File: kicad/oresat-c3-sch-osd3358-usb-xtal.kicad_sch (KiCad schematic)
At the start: 36 parts, among them U1 OSD3358-512M-BSM, U11 RCLAMP0504FB, Y1 24MHz, Y2 Crystal

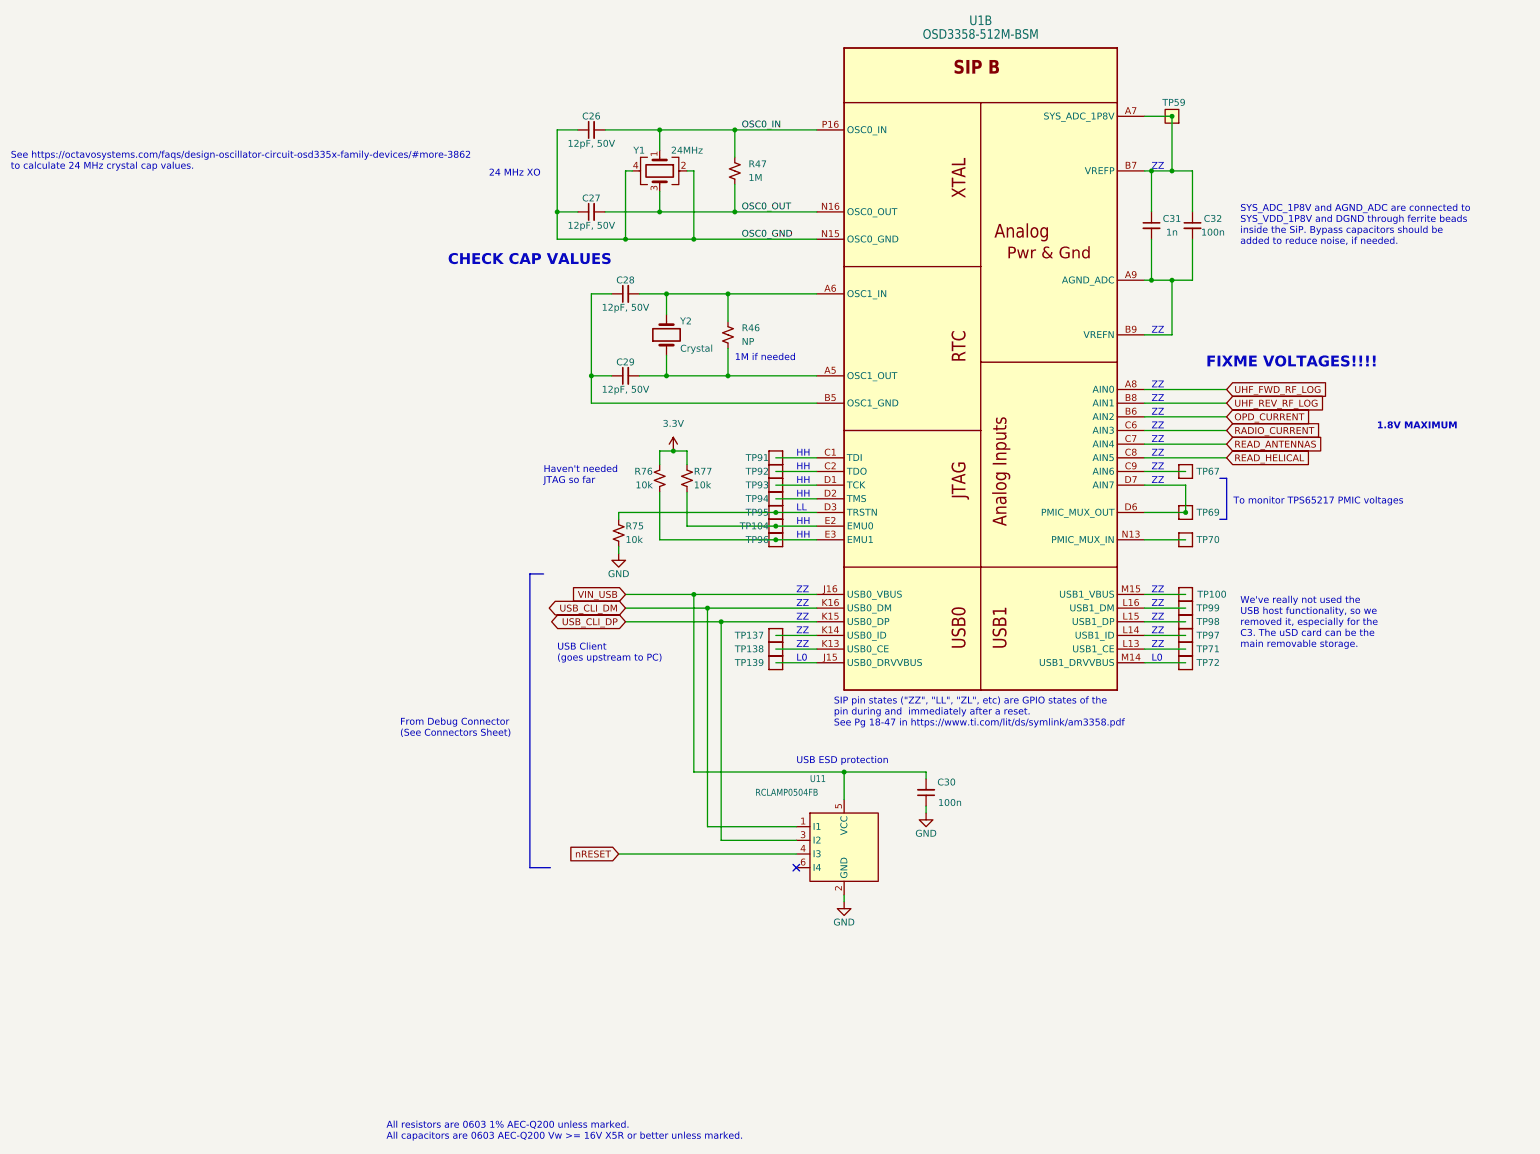
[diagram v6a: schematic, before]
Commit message: More fixes. TOT_CLEAR moved to a non HH pin, cleaned up in2 zones, moved fiducials, set dv/dt on power switches, added HW ID (5 bits) rechecked ADC 1.8V limits and fixed resistor values to match.
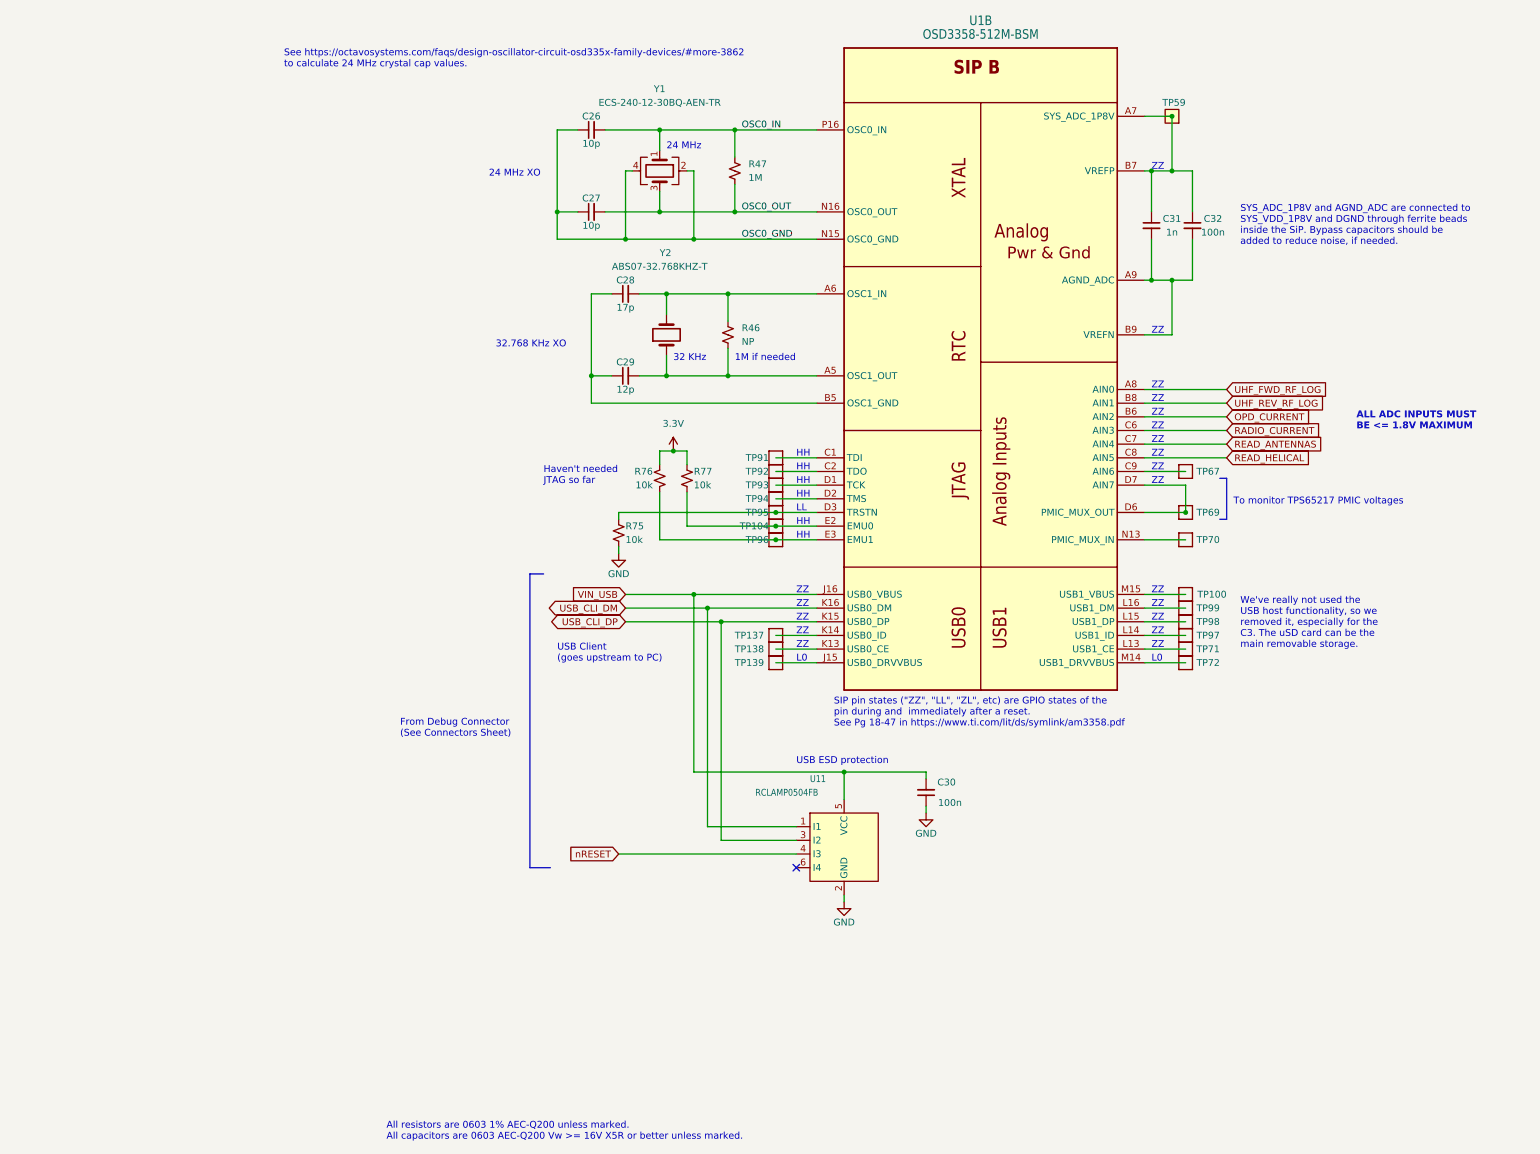
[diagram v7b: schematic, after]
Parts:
- C26, C27: value 12pF, 50V -> 10p
- C28: value 12pF, 50V -> 17p
- C29: value 12pF, 50V -> 12p
- Y1: value 24MHz -> ECS-240-12-30BQ-AEN-TR
- Y2: value Crystal -> ABS07-32.768KHZ-T
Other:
- note added: "24 MHz"
- note added: "32 KHz"
- note added: "32.768 KHz XO"
- note added: "ALL ADC INPUTS MUST BE <= 1.8V MAXIMUM"
- note removed: "1.8V MAXIMUM"
- note removed: "CHECK CAP VALUES"
- note removed: "FIXME VOLTAGES!!!!"
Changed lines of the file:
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@@
     (effects (font (size 1.27 1.27)) (justify left bottom))
   )
-  (text "1.8V MAXIMUM" (at 299.72 129.54 0)
+  (text "32.768 KHz XO" (at 135.89 114.3 0)
+    (effects (font (size 1.27 1.27)) (justify left bottom))
+  )
+  (text "ALL ADC INPUTS MUST\nBE <= 1.8V MAXIMUM" (at 295.91 129.54 0)
     (effects (font (size 1.27 1.27) (thickness 0.254) bold) (justify left bottom))
   )
@@
   (text "ZZ" (at 257.81 160.02 0)
     (effects (font (size 1.27 1.27)) (justify left bottom))
-  )
-  (text "FIXME VOLTAGES!!!!" (at 267.97 118.11 0)
-    (effects (font (size 2 2) (thickness 0.4) bold (color 255 0 0 1)) (justify left bottom))
   )
   (text "ZZ" (at 257.81 132.08 0)
@@
   )
   (text "See https://octavosystems.com/faqs/design-oscillator-circuit-osd335x-family-devices/#more-3862\nto calculate 24 MHz crystal cap values."
-    (at 45.72 81.28 0)
+    (at 96.52 62.23 0)
     (effects (font (size 1.27 1.27)) (justify left bottom))
   )
@@
     (effects (font (size 1.27 1.27)) (justify left bottom))
   )
-  (text "CHECK CAP VALUES" (at 127 99.06 0)
-    (effects (font (size 2 2) (thickness 0.4) bold (color 255 0 0 1)) (justify left bottom))
-  )
   (text "1M if needed" (at 180.34 116.84 0)
     (effects (font (size 1.27 1.27)) (justify left bottom))
@@
     (effects (font (size 1.27 1.27)) (justify left bottom))
   )
+  (text "32 KHz" (at 168.91 116.84 0)
+    (effects (font (size 1.27 1.27)) (justify left bottom))
+  )
   (text "HH" (at 191.77 134.62 0)
     (effects (font (size 1.27 1.27) (color 255 0 0 1)) (justify left bottom))
@@
   )
   (text "ZZ" (at 191.77 167.64 0)
+    (effects (font (size 1.27 1.27)) (justify left bottom))
+  )
+  (text "24 MHz" (at 167.64 77.47 0)
     (effects (font (size 1.27 1.27)) (justify left bottom))
   )
@@
   (symbol (lib_id "Device:Crystal_GND24") (at 166.37 81.28 270) (unit 1)
     (in_bom yes) (on_board yes) (dnp no)
-    (property "Reference" "Y1" (at 162.56 77.47 90)
-      (effects (font (size 1.27 1.27)))
-    )
-    (property "Value" "24MHz" (at 171.45 77.47 90)
+    (property "Reference" "Y1" (at 166.37 66.04 90)
+      (effects (font (size 1.27 1.27)))
+    )
+    (property "Value" "ECS-240-12-30BQ-AEN-TR" (at 166.37 68.58 90)
       (effects (font (size 1.27 1.27)))
     )
@@
       (effects (font (size 1.27 1.27)) hide)
     )
-    (property "Datasheet" "~" (at 166.37 81.28 0)
+    (property "Datasheet" "https://ecsxtal.com/store/pdf/ECX-53BQ.pdf" (at 166.37 81.28 0)
       (effects (font (size 1.27 1.27)) hide)
     )
@@
   (symbol (lib_id "Device:Crystal") (at 167.64 111.76 90) (unit 1)
     (in_bom yes) (on_board yes) (dnp no)
-    (property "Reference" "Y2" (at 170.18 109.22 90)
+    (property "Reference" "Y2" (at 166.37 96.52 90)
       (effects (font (size 1.27 1.27)) (justify right))
     )
-    (property "Value" "Crystal" (at 170.18 114.3 90)
+    (property "Value" "ABS07-32.768KHZ-T" (at 157.48 99.06 90)
       (effects (font (size 1.27 1.27)) (justify right))
     )
@@
       (effects (font (size 1.27 1.27)) hide)
     )
-    (property "Datasheet" "~" (at 167.64 111.76 0)
+    (property "Datasheet" "https://abracon.com/Resonators/ABS07.pdf" (at 167.64 111.76 0)
       (effects (font (size 1.27 1.27)) hide)
     )
@@
       (effects (font (size 1.27 1.27)))
     )
-    (property "Value" "12pF, 50V" (at 153.67 91.44 90)
+    (property "Value" "10p" (at 153.67 91.44 90)
       (effects (font (size 1.27 1.27)))
     )
@@
       (effects (font (size 1.27 1.27)))
     )
-    (property "Value" "12pF, 50V" (at 160.02 121.92 90)
+    (property "Value" "12p" (at 160.02 121.92 90)
       (effects (font (size 1.27 1.27)))
     )
@@
       (effects (font (size 1.27 1.27)))
     )
-    (property "Value" "12pF, 50V" (at 160.02 106.68 90)
+    (property "Value" "17p" (at 160.02 106.68 90)
       (effects (font (size 1.27 1.27)))
     )
@@
       (effects (font (size 1.27 1.27)))
     )
-    (property "Value" "12pF, 50V" (at 153.67 76.2 90)
-      (effects (font (size 1.27 1.27)))
-    )
+    (property "Value" "10p" (at 153.67 76.2 90)
+      (effects (font (size 1.27 1.27)))
+    )

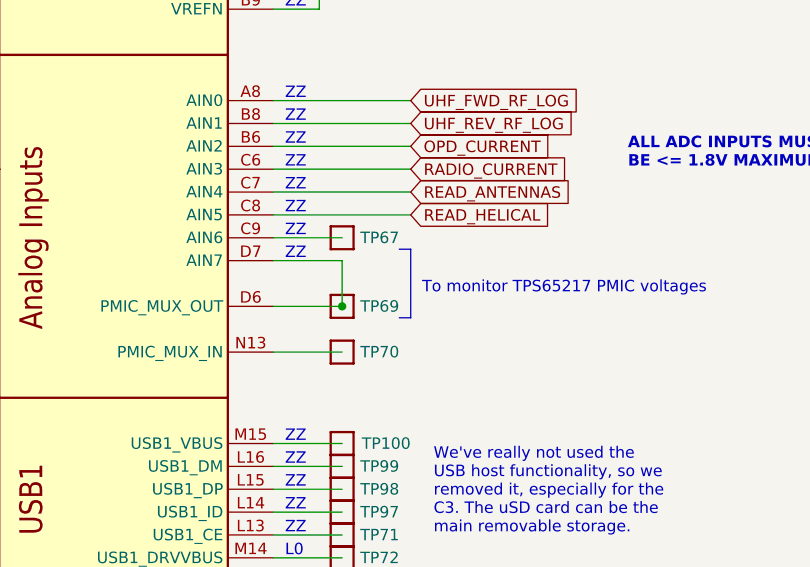
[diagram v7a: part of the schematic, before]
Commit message: Updated AX5043 foot print, moved synthesize to correct L length, fixed more grounds
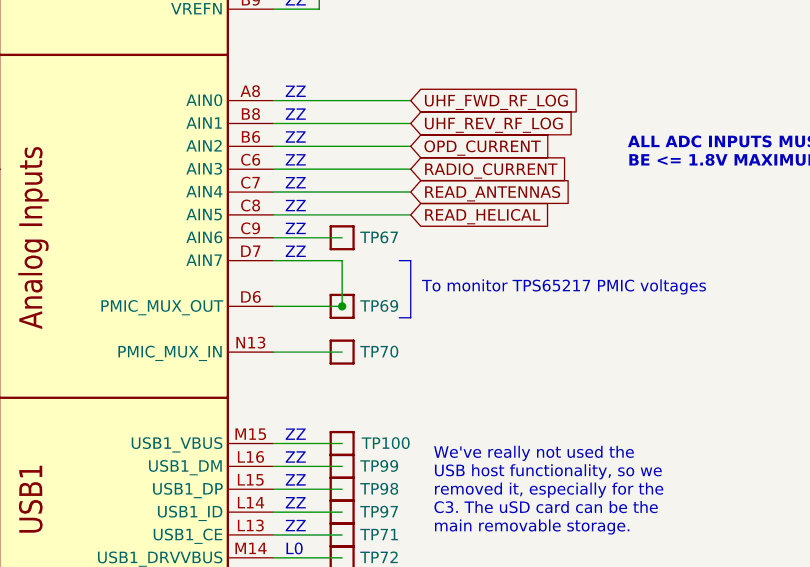
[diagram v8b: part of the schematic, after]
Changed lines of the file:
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@@
   )
   (no_connect (at 191.77 210.82))
-  (polyline (pts (xy 271.78 138.43) (xy 271.78 146.05))
+  (polyline (pts (xy 271.78 139.7) (xy 271.78 146.05))
     (stroke (width 0) (type default))
   )
@@
     (stroke (width 0) (type default))
   )
-  (polyline (pts (xy 270.51 138.43) (xy 271.78 138.43))
-    (stroke (width 0) (type default))
-  )
+  (polyline (pts (xy 270.51 139.7) (xy 271.78 139.7))
+    (stroke (width 0) (type default))
+  )
